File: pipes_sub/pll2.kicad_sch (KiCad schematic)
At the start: 86 parts, among them U12 CD4046, U14 CD4017, U16 CD4046, U17 CD4046, U18 CD4017, U19 CD4017, U38 TL072CP, U39 TL072CP, U4 CD4046, U7 CD4017

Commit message: Adds digikey bom merge. Uses local graphics for panel.
Adds bambooh graphics
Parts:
- added R149, R150, R153, R154: 300K, Resistor_SMD:R_0603_1608Metric, symbol Device:R_Small_US
- added R151, R152, R155, R156: 249K, Resistor_SMD:R_0603_1608Metric, symbol Device:R_Small_US
- C14, C22, C27, C28: value 1nF -> 300p; LCSC Part # C46653 -> C282698
- C17, C25, C37, C38: value 1uF -> 10uF; LCSC Part # C28323 -> C15850
- R100, R104, R120, R124: value 300K -> 150K; LCSC Part # C23024 -> C22807
- R101, R105, R121, R125: value 200K -> 165K; LCSC Part # C25811 -> C308203
- R102, R106, R122, R126: value 150K -> 249K; LCSC Part # C22807 -> C311921
- R107, R112, R127, R132: value 274K -> 165K; LCSC Part # C227748 -> C308203
- R108, R113, R128, R133: value 274K -> 150K; LCSC Part # C227748 -> C22807
- R109, R114, R129, R134: value 158K -> 200K; LCSC Part # C273745 -> C25811
- R110, R115, R130, R135: value 158K -> 300K; LCSC Part # C273745 -> C23024
- R20, R31, R38, R39: value 24.9K -> 10K; LCSC Part # C137761 -> C25804
- R23, R36, R40, R42: value 200K -> 27K; LCSC Part # C17539 -> C17593
- R24, R37, R41, R43: value 10K -> 1.5K; LCSC Part # C17414 -> C4310
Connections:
- net GND: now also U14.15 (Reset), U18.15 (Reset), U19.15 (Reset), U7.15 (Reset)
- net at R123.2, R124.2, R125.2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: now also R154.2, R156.2
- net at R103.2, R104.2, R105.2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: now also R150.2, R152.2
- net at R119.2, R120.2, R121.2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: now also R153.2, R155.2
- net at U7.11 (Q9): now also R156.1
- net at U7.9 (Q8): now also R154.1; no longer U7.15 (Reset)
- net at R100.2, R101.2, R102.2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: now also R149.2, R151.2
- net at U18.11 (Q9): now also R155.1
- net at U18.9 (Q8): now also R153.1; no longer U18.15 (Reset)
- net at U14.11 (Q9): now also R152.1
- net at U14.9 (Q8): now also R150.1; no longer U14.15 (Reset)
- net at U19.11 (Q9): now also R151.1
- net at U19.9 (Q8): now also R149.1; no longer U19.15 (Reset)
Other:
- moved on the sheet: R111, R116, R131, R136

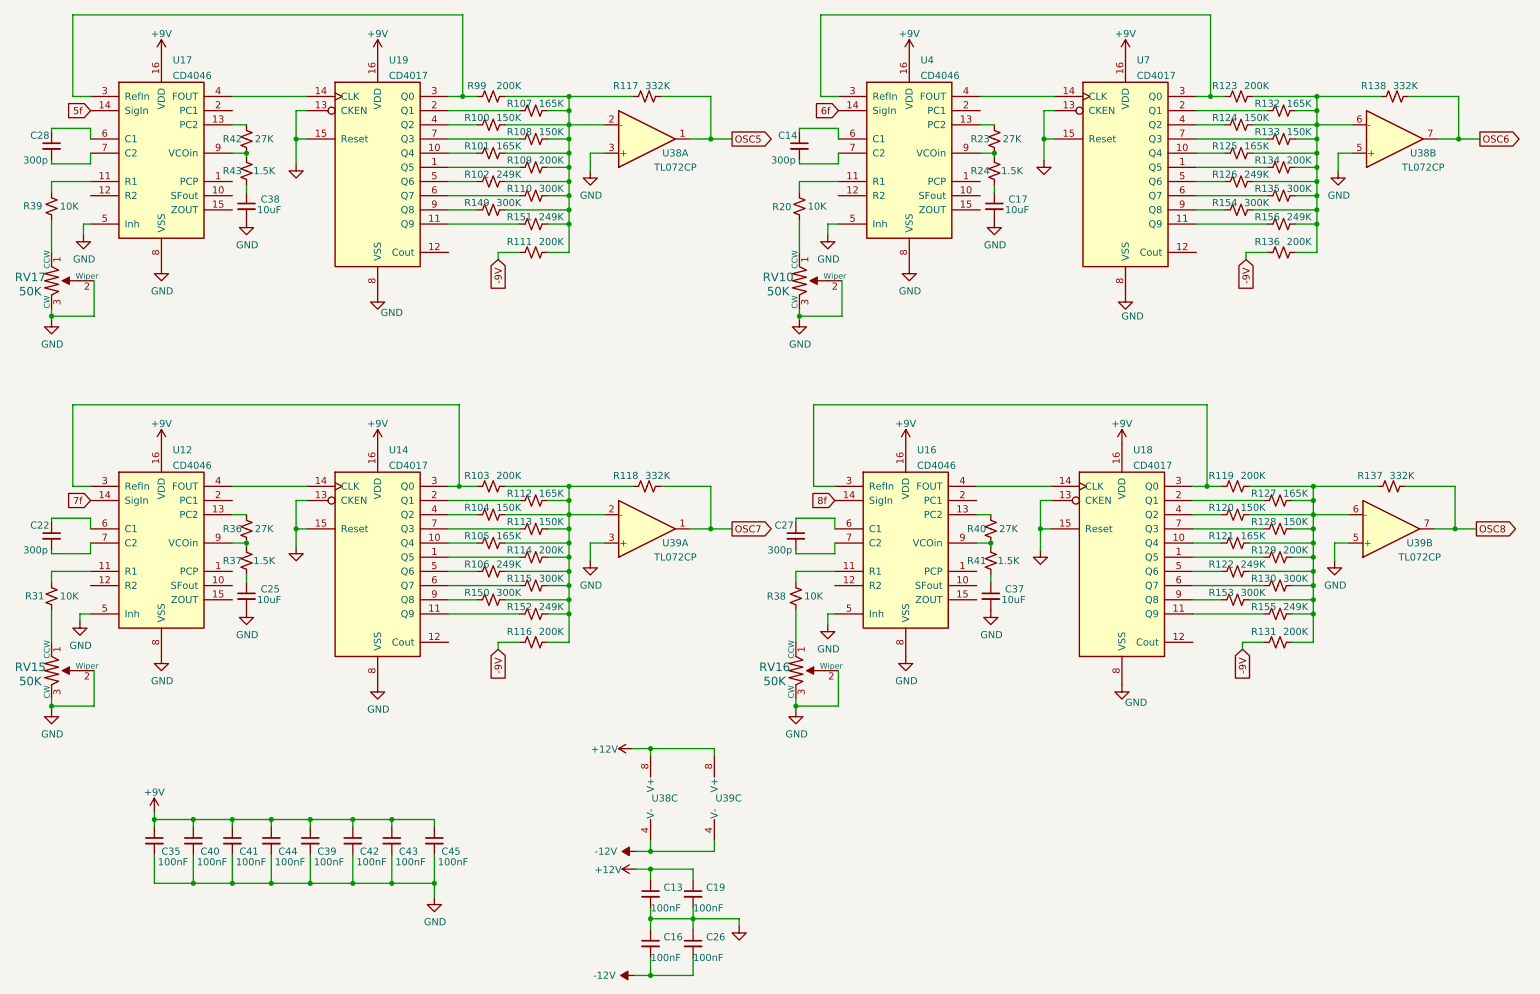
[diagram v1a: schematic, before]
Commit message: Version 1.1 of boards
Changes to use NSL-32SR3 Vactrols
Fixes 3904 package
Adds 10-step waveform
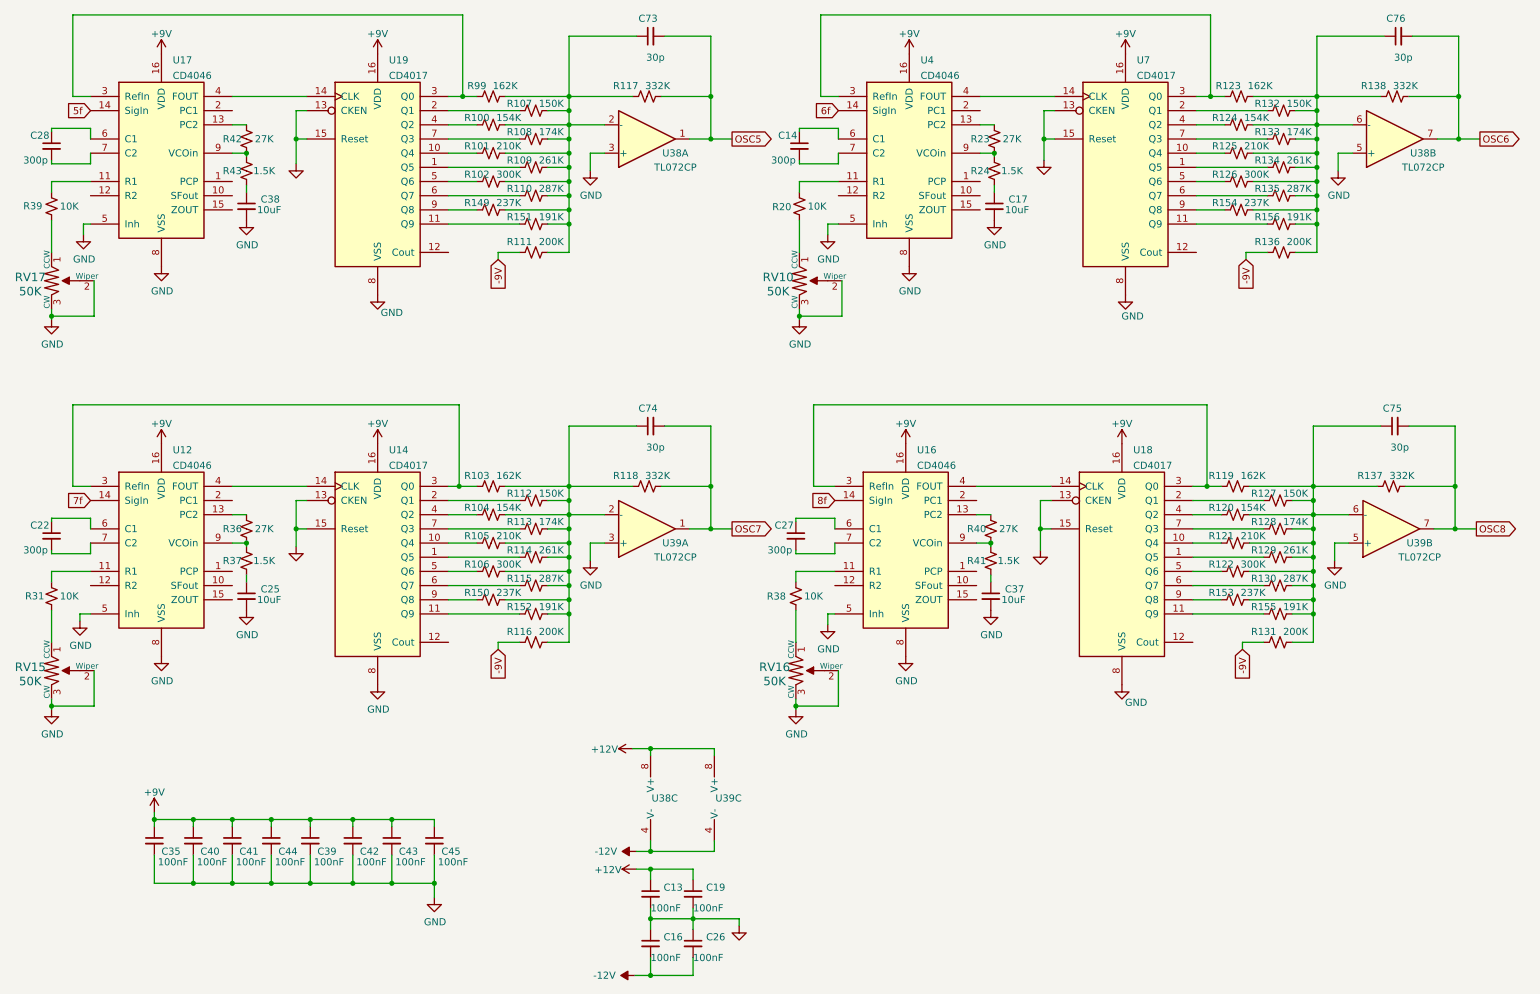
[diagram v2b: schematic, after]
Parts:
- added C73, C74, C75, C76: 30p, Capacitor_SMD:C_0805_2012Metric_Pad1.18x1.45mm_HandSolder, symbol Device:C_Small
- R100, R104, R120, R124: value 150K -> 154K; LCSC Part # C22807 -> C321731
- R101, R105, R121, R125: value 165K -> 210K; LCSC Part # C308203 -> C227705
- R102, R106, R122, R126: value 249K -> 300K; LCSC Part # C311921 -> C23024
- R103, R119, R123, R99: value 200K -> 162K; LCSC Part # C25811 -> C217756
- R107, R112, R127, R132: value 165K -> 150K; LCSC Part # C308203 -> C22807
- R108, R113, R128, R133: value 150K -> 174K; LCSC Part # C22807 -> C2933159
- R109, R114, R129, R134: value 200K -> 261K; LCSC Part # C25811 -> C2930083
- R110, R115, R130, R135: value 300K -> 287K; LCSC Part # C23024 -> C5159700
- R149, R150, R153, R154: value 300K -> 237K; LCSC Part # C23024 -> C403089
- R151, R152, R155, R156: value 249K -> 191K; LCSC Part # C311921 -> C861179
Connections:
- net OSC5: now also C73.2
- net OSC6: now also C76.2
- net OSC7: now also C74.2
- net OSC8: now also C75.2
- net at R123.2, R124.2, R125.2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: now also C76.1
- net at R103.2, R104.2, R105.2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: now also C74.1
- net at R119.2, R120.2, R121.2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: now also C75.1
- net at R100.2, R101.2, R102.2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: now also C73.1
